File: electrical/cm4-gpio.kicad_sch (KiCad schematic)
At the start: 1 part

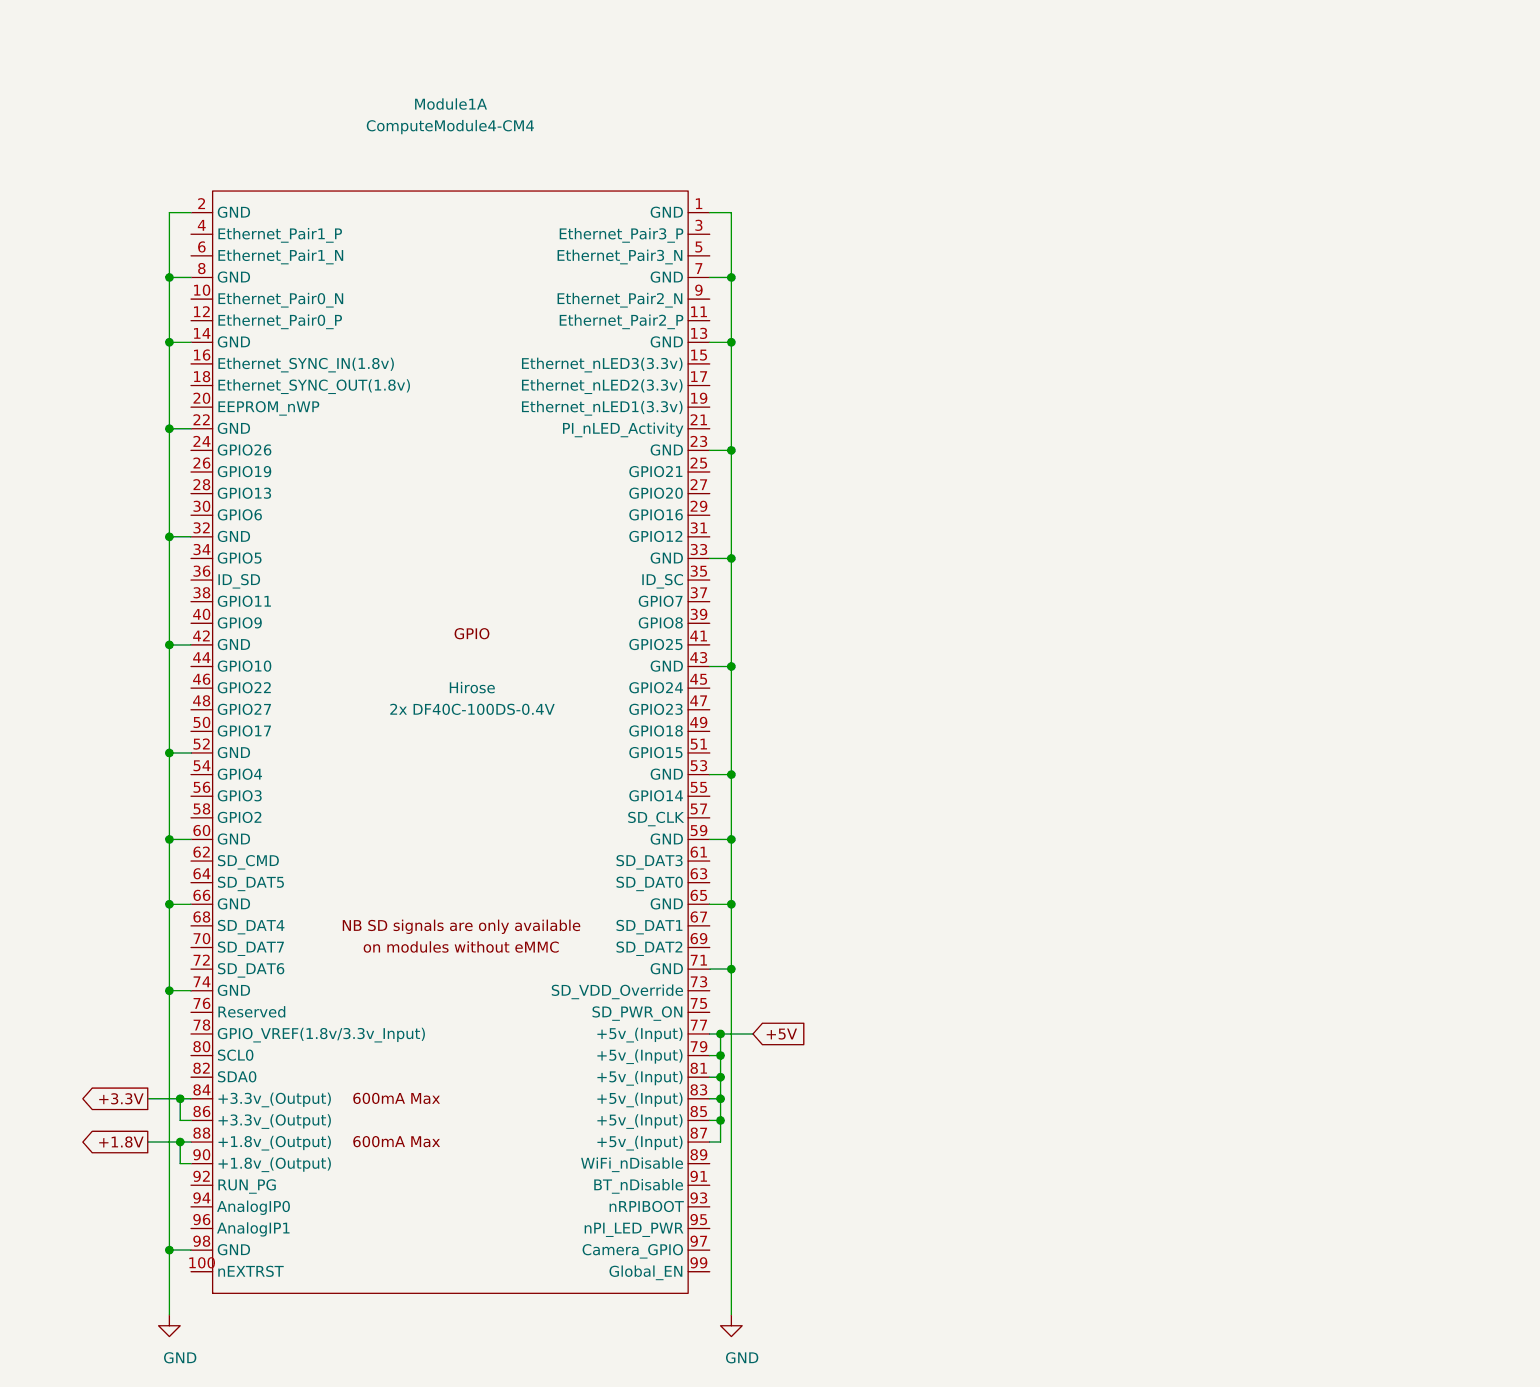
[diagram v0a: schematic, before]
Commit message: Add Pi LEDs + center tap connections
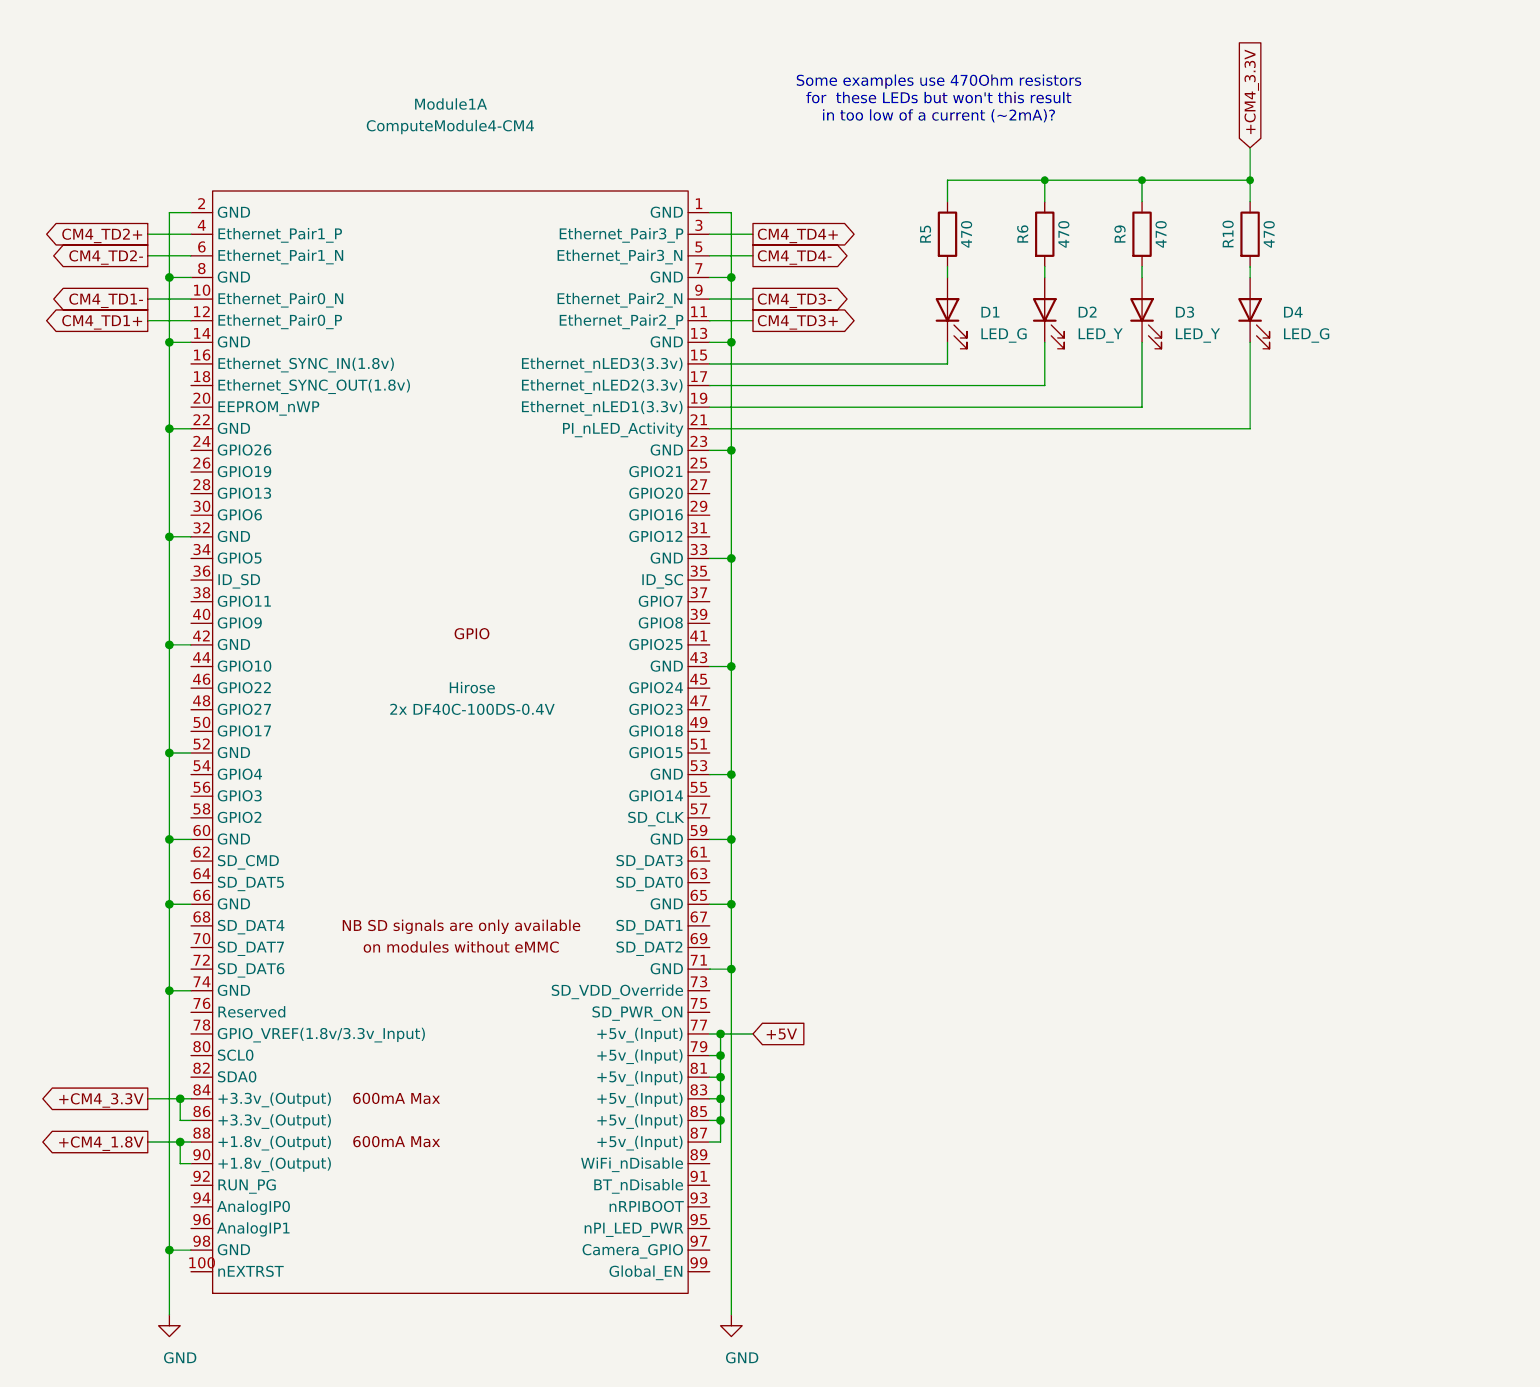
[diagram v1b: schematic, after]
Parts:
- added D1, D4: LED_G, symbol Device:LED
- added D2, D3: LED_Y, symbol Device:LED
- added R10, R5, R6, R9: 470, symbol Device:R
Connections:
- net CM4_TD1-: now reaches Module1.10 (Ethernet_Pair0_N)
- net CM4_TD3+: now reaches Module1.11 (Ethernet_Pair2_P)
- net CM4_TD1+: now reaches Module1.12 (Ethernet_Pair0_P)
- net at Module1.15 (Ethernet_nLED3(3.3v)): now also D1.1 (K)
- net at Module1.17 (Ethernet_nLED2(3.3v)): now also D2.1 (K)
- net at Module1.19 (Ethernet_nLED1(3.3v)): now also D3.1 (K)
- net at Module1.21 (PI_nLED_Activity): now also D4.1 (K)
- net CM4_TD4+: now reaches Module1.3 (Ethernet_Pair3_P)
- net CM4_TD2+: now reaches Module1.4 (Ethernet_Pair1_P)
- net CM4_TD4-: now reaches Module1.5 (Ethernet_Pair3_N)
- net CM4_TD2-: now reaches Module1.6 (Ethernet_Pair1_N)
- net CM4_TD3-: now reaches Module1.9 (Ethernet_Pair2_N)
- net +1.8V renamed +CM4_1.8V
- net +3.3V renamed +CM4_3.3V
- net +CM4_3.3V: now also R10.1, R5.1, R6.1, R9.1
- new net: D4.2 (A), R10.2
- new net: D1.2 (A), R5.2
- new net: D2.2 (A), R6.2
- new net: D3.2 (A), R9.2
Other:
- note added: "Some examples use 470Ohm resistors for these LEDs but won't this result in too low of a current (~2mA)?"

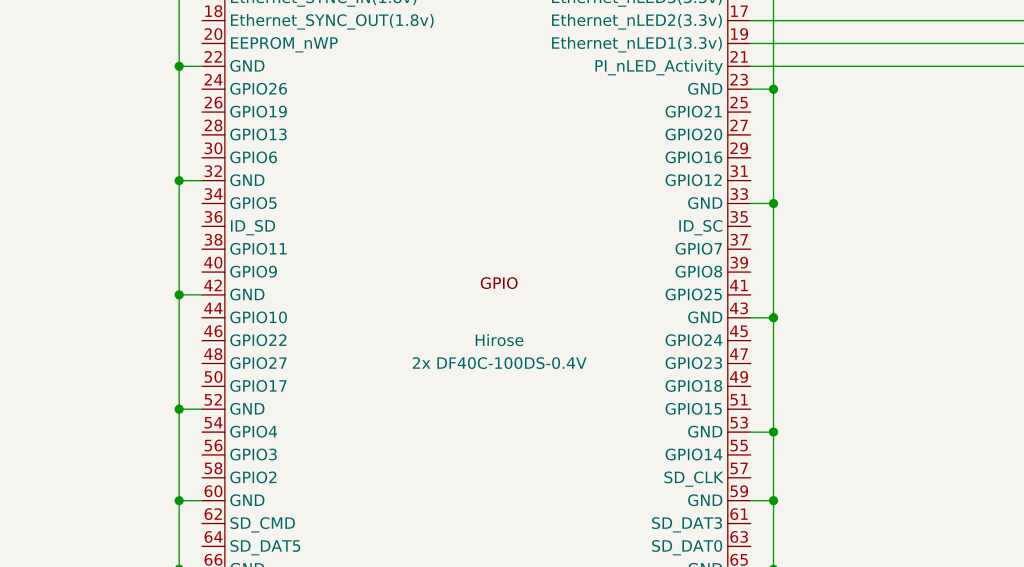
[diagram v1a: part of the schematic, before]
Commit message: Pi <-> Switch SPI interface
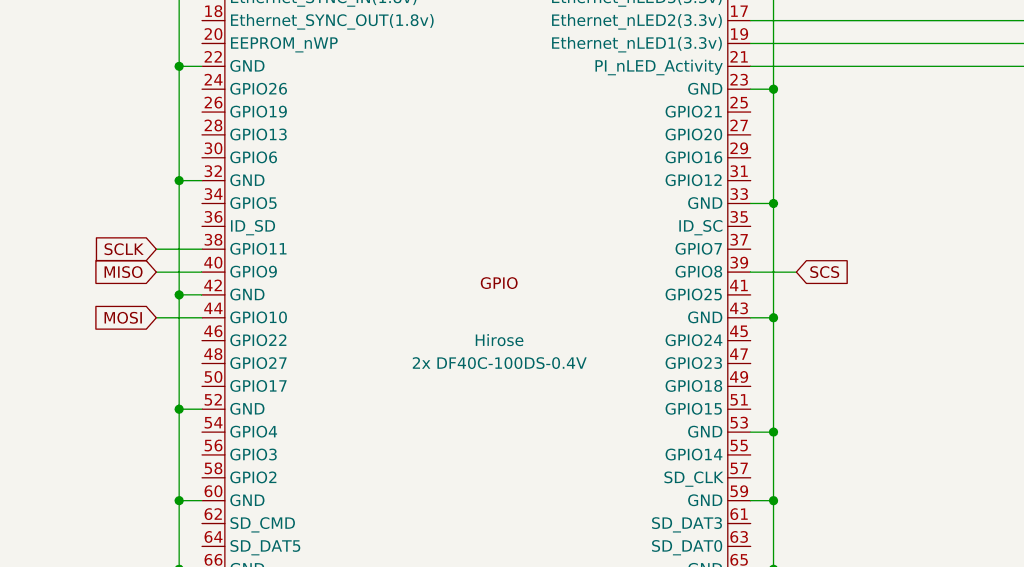
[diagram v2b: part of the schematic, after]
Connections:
- net SCLK: now reaches Module1.38 (GPIO11)
- net SCS: now reaches Module1.39 (GPIO8)
- net MISO: now reaches Module1.40 (GPIO9)
- net MOSI: now reaches Module1.44 (GPIO10)
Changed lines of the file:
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@@
+	(wire
+		(pts
+			(xy 38.1 99.06) (xy 43.18 99.06)
+		)
+		(stroke
+			(width 0)
+			(type default)
+		)
+	)
 	(wire
 		(pts
@@
 	(wire
 		(pts
+			(xy 104.14 93.98) (xy 109.22 93.98)
+		)
+		(stroke
+			(width 0)
+			(type default)
+		)
+	)
+	(wire
+		(pts
 			(xy 104.14 60.96) (xy 106.68 60.96)
 		)
@@
 	(wire
 		(pts
+			(xy 38.1 91.44) (xy 43.18 91.44)
+		)
+		(stroke
+			(width 0)
+			(type default)
+		)
+	)
+	(wire
+		(pts
 			(xy 104.14 45.72) (xy 106.68 45.72)
 		)
@@
 			(width 0)
 			(type solid)
+		)
+	)
+	(wire
+		(pts
+			(xy 38.1 93.98) (xy 43.18 93.98)
+		)
+		(stroke
+			(width 0)
+			(type default)
 		)
 	)
@@
 		)
 	)
+	(global_label "MISO"
+		(shape input)
+		(at 38.1 93.98 180)
+		(fields_autoplaced yes)
+		(effects
+			(font
+				(size 1.27 1.27)
+			)
+			(justify right)
+		)
+		(property "Intersheetrefs" "${INTERSHEET_REFS}"
+			(at 30.4235 93.98 0)
+			(effects
+				(font
+					(size 1.27 1.27)
+				)
+				(justify right)
+				(hide yes)
+			)
+		)
+	)
 	(global_label "CM4_TD2+"
 		(shape output)
@@
 		)
 	)
+	(global_label "SCLK"
+		(shape input)
+		(at 38.1 91.44 180)
+		(fields_autoplaced yes)
+		(effects
+			(font
+				(size 1.27 1.27)
+			)
+			(justify right)
+		)
+		(property "Intersheetrefs" "${INTERSHEET_REFS}"
+			(at 30.2421 91.44 0)
+			(effects
+				(font
+					(size 1.27 1.27)
+				)
+				(justify right)
+				(hide yes)
+			)
+		)
+	)
 	(global_label "CM4_TD1+"
 		(shape output)
@@
 		)
 	)
+	(global_label "SCS"
+		(shape input)
+		(at 109.22 93.98 0)
+		(fields_autoplaced yes)
+		(effects
+			(font
+				(size 1.27 1.27)
+			)
+			(justify left)
+		)
+		(property "Intersheetrefs" "${INTERSHEET_REFS}"
+			(at 115.9893 93.98 0)
+			(effects
+				(font
+					(size 1.27 1.27)
+				)
+				(justify left)
+				(hide yes)
+			)
+		)
+	)
 	(global_label "CM4_TD4-"
 		(shape output)
@@
 				(hide yes)
 			)
+		)
+	)
+	(global_label "MOSI"
+		(shape input)
+		(at 38.1 99.06 180)
+		(fields_autoplaced yes)
+		(effects
+			(font
+				(size 1.27 1.27)
+			)
+			(justify right)
+		)
+		(property "Intersheetrefs" "${INTERSHEET_REFS}"
+			(at 30.4235 99.06 0)
+			(effects
+				(font
+					(size 1.27 1.27)
+				)
+				(justify right)
+				(hide yes)
+			)
